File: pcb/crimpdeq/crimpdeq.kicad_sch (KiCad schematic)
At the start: 55 parts, among them J10 A-_Cable_Pad, J11 E+_Cable_Pad, J12 E-_Cable_Pad, J2 USB4105-GF-A, J5 B-_Cable_Pad, J6 SW+_Cable_Pad, J7 B+_Cable_Pad, J8 SW-_Cable_Pad, J9 A+_Cable_Pad, Q2 DMG3415U, U1 ESP32-C3-MINI-1, U2 MCP73831T-2ACI/OT, U3 ADS1220, U5 MAX17048G+T10, U6 SY8088

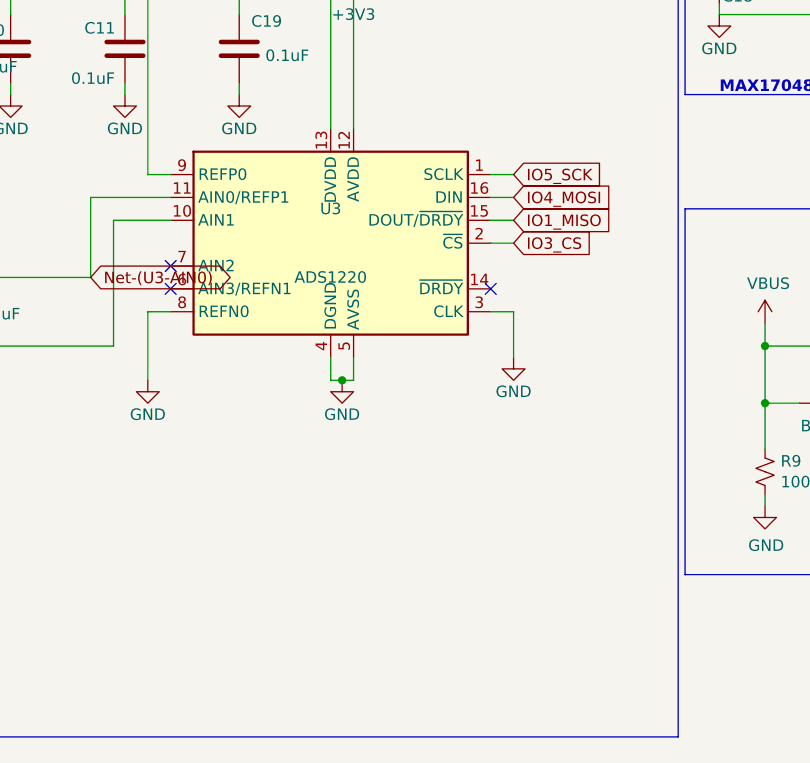
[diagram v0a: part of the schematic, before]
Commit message: fix: add ADC SPI damping and C0G filter
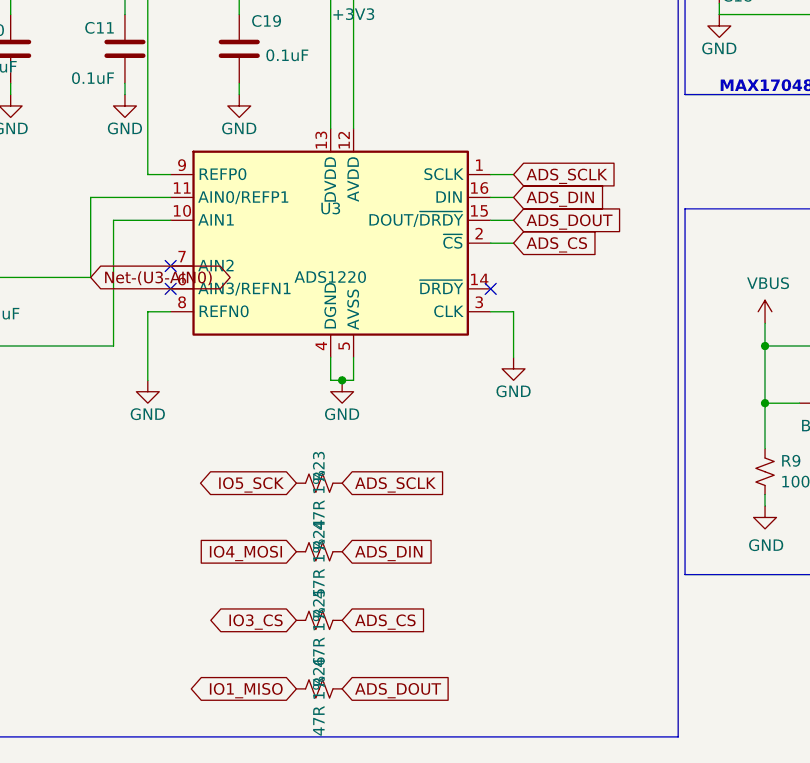
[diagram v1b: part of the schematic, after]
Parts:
- added R23, R24, R25, R26: 47R 1%, Resistor_SMD:R_0402_1005Metric, symbol Device:R_Small_US
- C12: footprint Capacitor_SMD:C_0603_1608Metric -> Capacitor_SMD:C_1206_3216Metric; LCSC (none) -> C405303; MPN (none) -> GRM31C5C2A104JA01L; Manufacturer (none) -> Murata
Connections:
- net IO1_MISO: now also R26.2; no longer U3.15 (DOUT/~{DRDY})
- net IO3_CS: now also R25.1; no longer U3.2 (~{CS})
- net IO4_MOSI: now also R24.1; no longer U3.16 (DIN)
- net IO5_SCK: now also R23.1; no longer U3.1 (SCLK)
- new net ADS_CS: R25.2, U3.2 (~{CS})
- new net ADS_DIN: R24.2, U3.16 (DIN)
- new net ADS_DOUT: R26.1, U3.15 (DOUT/~{DRDY})
- new net ADS_SCLK: R23.2, U3.1 (SCLK)

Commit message: fix: reconcile PCB and schematic libraries
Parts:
- C11, C19: footprint C_0603_1608Metric -> Capacitor_SMD:C_0603_1608Metric
- D4: LCSC (none) -> C52917433; MANUFACTURER (none) -> Worldsemi; MPN (none) -> WS2812B-V6
- J2: footprint Rust_Board:GCT_USB4105-GF-A -> Crimpdeq:GCT_USB4105-GF-A; symbol Rust_Board:USB4105-GF-A -> Crimpdeq:USB4105-GF-A; MPN (none) -> USB4105-GF-A
- Q2: footprint Package_TO_SOT_SMD:SOT-23 -> Crimpdeq:SOT-23; MANUFACTURER (none) -> Diodes Incorporated; MPN (none) -> DMG3415U-7
- U1: footprint PCM_Espressif:ESP32-C3-MINI-1 -> Crimpdeq:ESP32-C3-MINI-1; symbol Espressif:ESP32-C3-MINI-1 -> Crimpdeq:ESP32-C3-MINI-1; MANUFACTURER (none) -> Espressif Systems; MPN (none) -> ESP32-C3-MINI-1
- U2: footprint Package_TO_SOT_SMD:SOT-23-5 -> Crimpdeq:MCP73831_SOT-23-5
- U3: footprint TSSOP-16_4.4x5mm_P0.65mm -> Package_SO:TSSOP-16_4.4x5mm_P0.65mm; LCSC (none) -> C48263; MANUFACTURER (none) -> Texas Instruments; MPN (none) -> ADS1220IPWR
- U5: symbol Battery_Management:MAX17048 -> Crimpdeq:MAX17048; LCSC (none) -> C2682616; MANUFACTURER (none) -> Analog Devices / Maxim Integrated; MPN (none) -> MAX17048G+T10
- U6: footprint Package_TO_SOT_SMD:SOT-23-5 -> Crimpdeq:SY8088_SOT-23-5; symbol Rust_Board:SY8088 -> Crimpdeq:SY8088
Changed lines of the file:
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@@
 			)
 		)
-		(property "Footprint" "Package_TO_SOT_SMD:SOT-23-5"
+		(property "Footprint" "Crimpdeq:MCP73831_SOT-23-5"
 			(at 152.4 43.18 0)
 			(hide yes)
@@
 			)
 		)
-		(property "Footprint" "Package_TO_SOT_SMD:SOT-23"
+		(property "Footprint" "Crimpdeq:SOT-23"
 			(at 151.13 155.575 0)
 			(hide yes)
@@
 			)
 		)
-		(property "Datasheet" "https://www.diodes.com/assets/Datasheets/DMG2301L.pdf"
+		(property "Datasheet" "https://www.diodes.com/assets/Datasheets/DMG3415U.pdf"
 			(at 146.05 153.67 0)
 			(hide yes)
@@
 			)
 		)
-	)
+		(property "MANUFACTURER" "Diodes Incorporated"
+			(at 146.05 153.67 0)
+			(hide yes)
+			(effects
+				(font
+					(size 1.27 1.27)
+				)
+			)
+		)
+		(property "MPN" "DMG3415U-7"
+			(at 146.05 153.67 0)
+			(hide yes)
+			(effects
+				(font
+					(size 1.27 1.27)
+				)
+			)
+		))
 	(symbol
 		(lib_id "Connector_Generic:Conn_01x01")
@@
 			)
 		)
-		(property "Footprint" "TSSOP-16_4.4x5mm_P0.65mm"
+		(property "Footprint" "Package_SO:TSSOP-16_4.4x5mm_P0.65mm"
 			(at 82.55 142.24 0)
 			(hide yes)
@@
 			)
 		)
-		(property "Datasheet" ""
+		(property "Datasheet" "https://www.ti.com/lit/ds/symlink/ads1220.pdf"
 			(at 82.55 142.24 0)
 			(hide yes)
@@
 			)
 		)
-	)
+		(property "LCSC" "C48263"
+			(at 82.55 142.24 0)
+			(hide yes)
+			(effects
+				(font
+					(size 1.27 1.27)
+				)
+			)
+		)
+		(property "MANUFACTURER" "Texas Instruments"
+			(at 82.55 142.24 0)
+			(hide yes)
+			(effects
+				(font
+					(size 1.27 1.27)
+				)
+			)
+		)
+		(property "MPN" "ADS1220IPWR"
+			(at 82.55 142.24 0)
+			(hide yes)
+			(effects
+				(font
+					(size 1.27 1.27)
+				)
+			)
+		))
 	(symbol
 		(lib_id "Device:R_Small_US")
@@
 	)
 	(symbol
-		(lib_id "Espressif:ESP32-C3-MINI-1")
+		(lib_id "Crimpdeq:ESP32-C3-MINI-1")
 		(at 85.09 53.34 0)
 		(unit 1)
@@
 			)
 		)
-		(property "Footprint" "PCM_Espressif:ESP32-C3-MINI-1"
+		(property "Footprint" "Crimpdeq:ESP32-C3-MINI-1"
 			(at 85.09 86.36 0)
 			(hide yes)
@@
 			)
 		)
-	)
+		(property "MANUFACTURER" "Espressif Systems"
+			(at 85.09 53.34 0)
+			(hide yes)
+			(effects
+				(font
+					(size 1.27 1.27)
+				)
+			)
+		)
+		(property "MPN" "ESP32-C3-MINI-1"
+			(at 85.09 53.34 0)
+			(hide yes)
+			(effects
+				(font
+					(size 1.27 1.27)
+				)
+			)
+		))
 	(symbol
 		(lib_id "power:+3V3")
@@
 	)
 	(symbol
-		(lib_id "Rust_Board:SY8088")
+		(lib_id "Crimpdeq:SY8088")
 		(at 226.06 83.82 0)
 		(unit 1)
@@
 			)
 		)
-		(property "Footprint" "Package_TO_SOT_SMD:SOT-23-5"
+		(property "Footprint" "Crimpdeq:SY8088_SOT-23-5"
 			(at 226.06 106.68 0)
 			(hide yes)
@@
 	)
 	(symbol
-		(lib_id "Rust_Board:USB4105-GF-A")
+		(lib_id "Crimpdeq:USB4105-GF-A")
 		(at 213.36 39.37 0)
 		(unit 1)
@@
 			)
 		)
-		(property "Footprint" "Rust_Board:GCT_USB4105-GF-A"
+		(property "Footprint" "Crimpdeq:GCT_USB4105-GF-A"
 			(at 220.98 64.77 0)
 			(hide yes)
@@
 			)
 		)
-		(property "Datasheet" ""
+		(property "Datasheet" "https://gct.co/files/drawings/usb4105.pdf"
 			(at 212.09 34.29 0)
 			(hide yes)
@@
 			)
 		)
-	)
+		(property "MPN" "USB4105-GF-A"
+			(at 213.36 39.37 0)
+			(hide yes)
+			(effects
+				(font
+					(size 1.27 1.27)
+				)
+			)
+		))
 	(symbol
 		(lib_id "power:GND")
@@
 			)
 		)
-		(property "Footprint" "C_0603_1608Metric"
+		(property "Footprint" "Capacitor_SMD:C_0603_1608Metric"
 			(at 59.69 120.65 0)
 			(hide yes)
@@
 			)
 		)
-		(property "Footprint" "C_0603_1608Metric"
+		(property "Footprint" "Capacitor_SMD:C_0603_1608Metric"
 			(at 72.39 120.65 0)
 			(hide yes)
@@
 			)
 		)
-		(property "Datasheet" "https://cdn-shop.adafruit.com/datasheets/WS2812B.pdf"
+		(property "Datasheet" "https://www.lcsc.com/datasheet/C52917433.pdf"
 			(at 149.86 85.725 0)
 			(hide yes)
@@
 			)
 		)
-	)
+		(property "LCSC" "C52917433"
+			(at 147.32 76.2 0)
+			(hide yes)
+			(effects
+				(font
+					(size 1.27 1.27)
+				)
+			)
+		)
+		(property "MANUFACTURER" "Worldsemi"
+			(at 147.32 76.2 0)
+			(hide yes)
+			(effects
+				(font
+					(size 1.27 1.27)
+				)
+			)
+		)
+		(property "MPN" "WS2812B-V6"
+			(at 147.32 76.2 0)
+			(hide yes)
+			(effects
+				(font
+					(size 1.27 1.27)
+				)
+			)
+		))
 	(symbol
 		(lib_id "Device:R_Small_US")
@@
 	)
 	(symbol
-		(lib_id "Battery_Management:MAX17048")
+		(lib_id "Crimpdeq:MAX17048")
 		(at 149.86 111.76 0)
 		(unit 1)
@@
 			)
 		)
-		(property "Datasheet" ""
+		(property "Datasheet" "https://www.analog.com/media/en/technical-documentation/data-sheets/MAX17048-MAX17049.pdf"
 			(at 149.86 111.76 0)
 			(hide yes)
@@
 			)
 		)
-	)
+		(property "LCSC" "C2682616"
+			(at 149.86 111.76 0)
+			(hide yes)
+			(effects
+				(font
+					(size 1.27 1.27)
+				)
+			)
+		)
+		(property "MANUFACTURER" "Analog Devices / Maxim Integrated"
+			(at 149.86 111.76 0)
+			(hide yes)
+			(effects
+				(font
+					(size 1.27 1.27)
+				)
+			)
+		)
+		(property "MPN" "MAX17048G+T10"
+			(at 149.86 111.76 0)
+			(hide yes)
+			(effects
+				(font
+					(size 1.27 1.27)
+				)
+			)
+		))
 	(symbol
 		(lib_id "Device:R_Small_US")

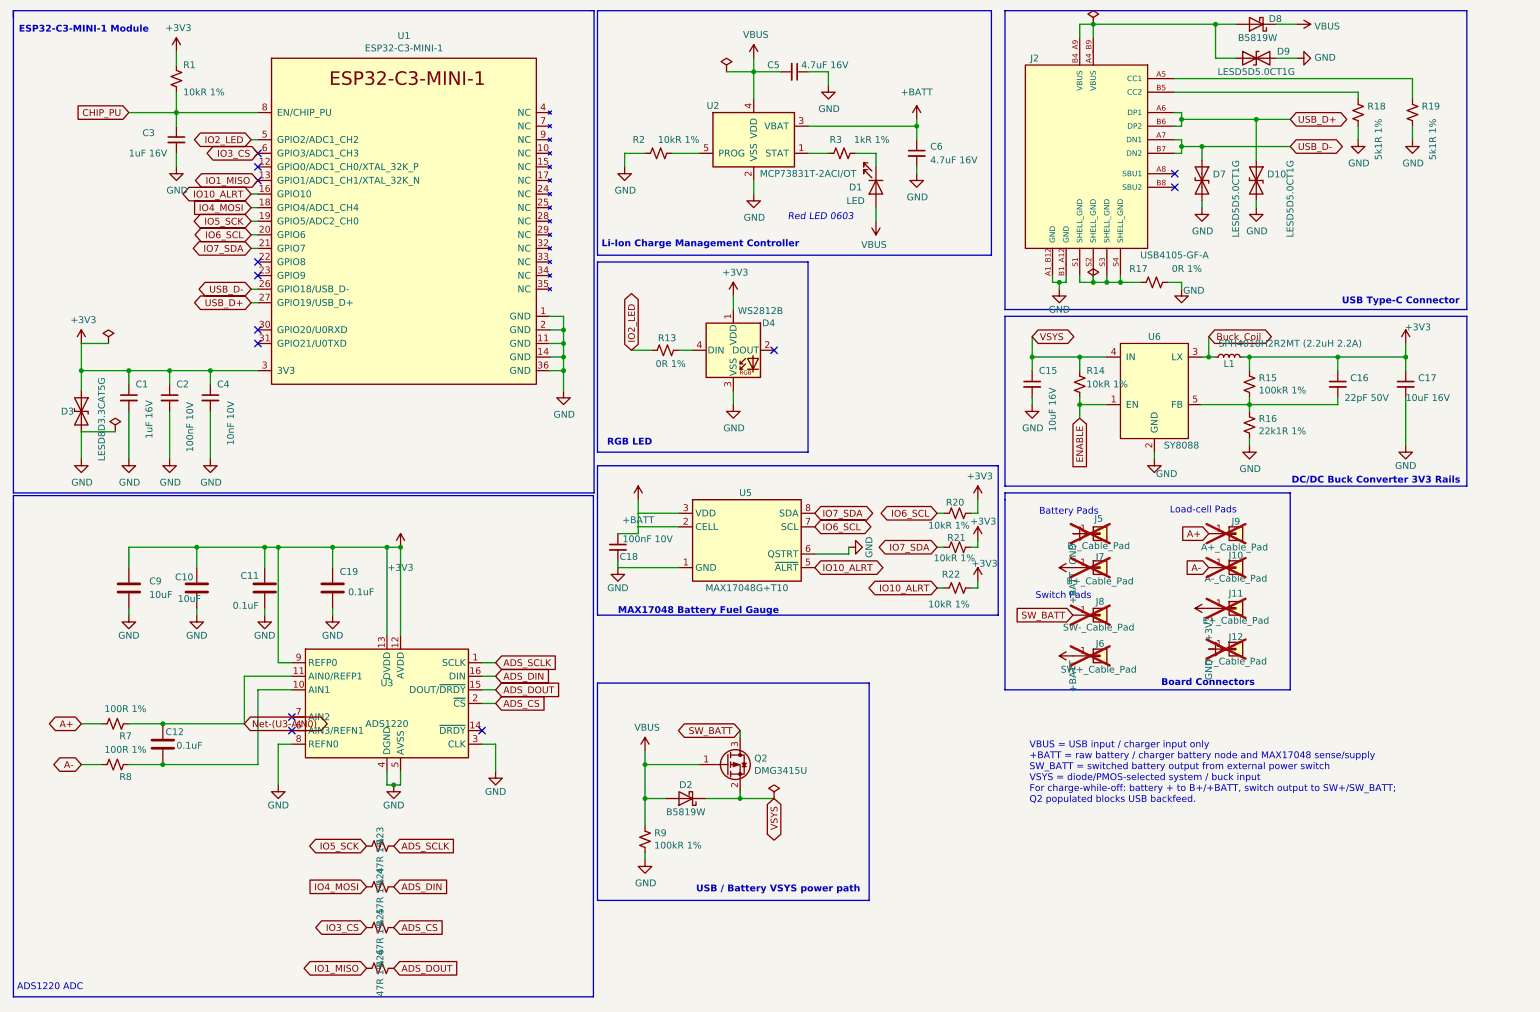
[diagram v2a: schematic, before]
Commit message: Revert "Revision 3 (#26)"
This reverts commit 90a500b67033c502f14e333f57f99a449d93ac6c.
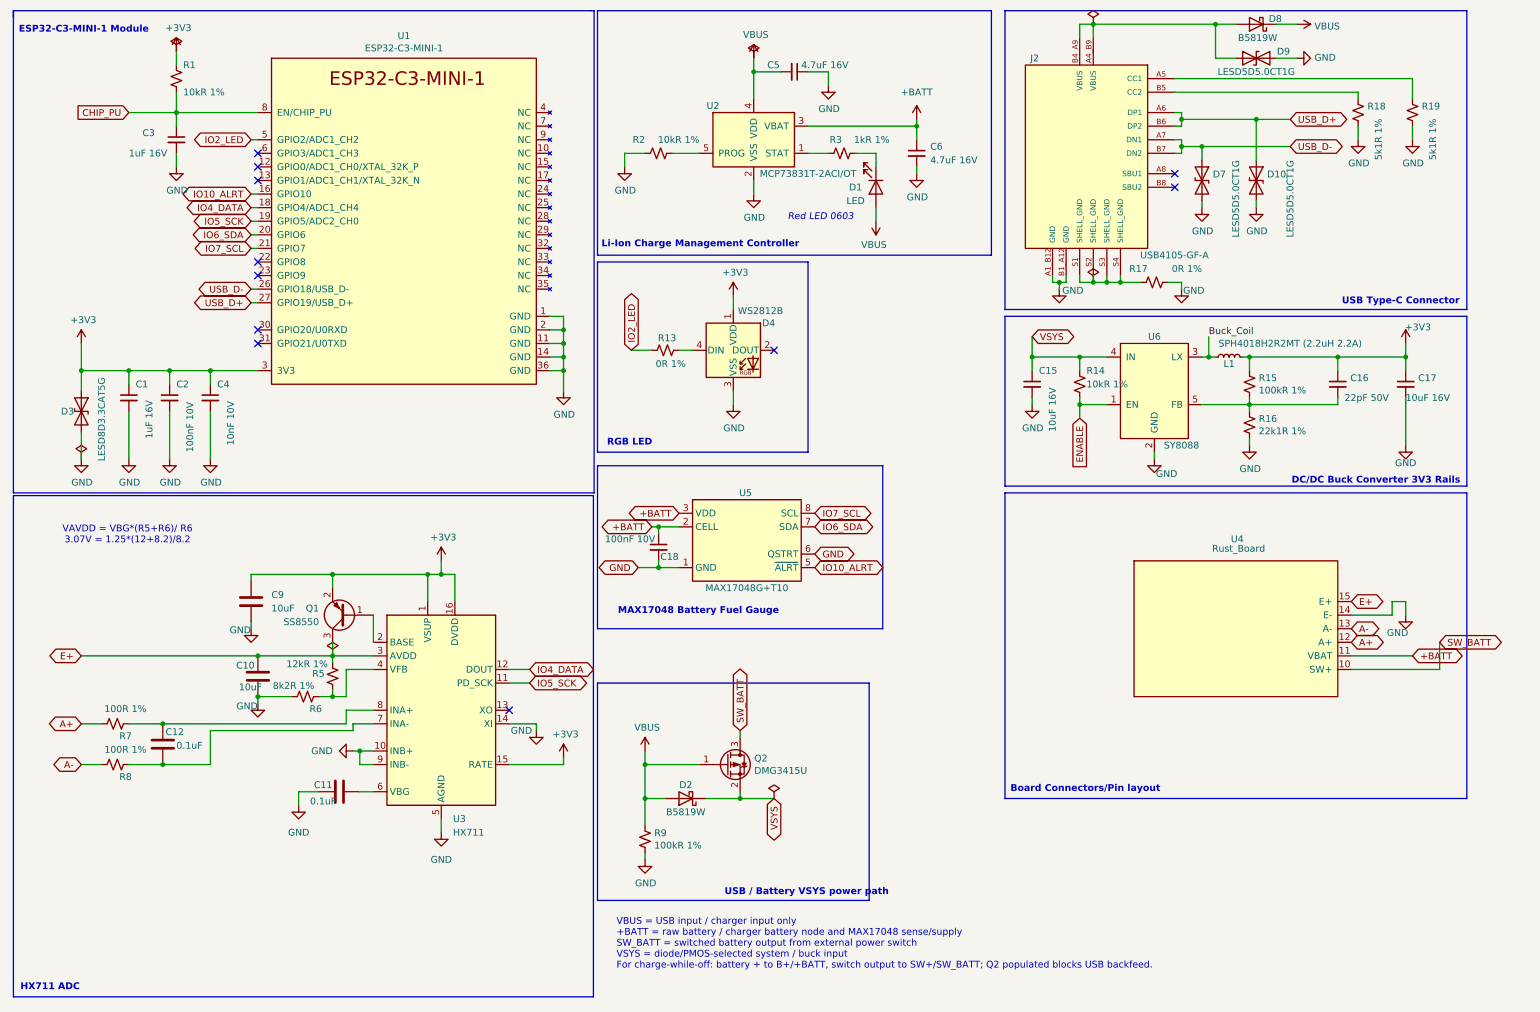
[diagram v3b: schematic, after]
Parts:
- removed C19: 0.1uF, Capacitor_SMD:C_0603_1608Metric, symbol Device:C
- removed J10: A-_Cable_Pad, TestPoint:TestPoint_THTPad_D1.5mm_Drill0.7mm, symbol Connector_Generic:Conn_01x01
- removed J11: E+_Cable_Pad, TestPoint:TestPoint_THTPad_D1.5mm_Drill0.7mm, symbol Connector_Generic:Conn_01x01
- removed J12: E-_Cable_Pad, TestPoint:TestPoint_THTPad_D1.5mm_Drill0.7mm, symbol Connector_Generic:Conn_01x01
- removed J5: B-_Cable_Pad, TestPoint:TestPoint_THTPad_D1.5mm_Drill0.7mm, symbol Connector_Generic:Conn_01x01
- removed J6: SW+_Cable_Pad, TestPoint:TestPoint_THTPad_D1.5mm_Drill0.7mm, symbol Connector_Generic:Conn_01x01
- removed J7: B+_Cable_Pad, TestPoint:TestPoint_THTPad_D1.5mm_Drill0.7mm, symbol Connector_Generic:Conn_01x01
- removed J8: SW-_Cable_Pad, TestPoint:TestPoint_THTPad_D1.5mm_Drill0.7mm, symbol Connector_Generic:Conn_01x01
- removed J9: A+_Cable_Pad, TestPoint:TestPoint_THTPad_D1.5mm_Drill0.7mm, symbol Connector_Generic:Conn_01x01
- removed R20, R21, R22: 10kR 1%, Resistor_SMD:R_0402_1005Metric, symbol Device:R_Small_US
- removed R23, R24, R25, R26: 47R 1%, Resistor_SMD:R_0402_1005Metric, symbol Device:R_Small_US
- removed U3: ADS1220, Package_SO:TSSOP-16_4.4x5mm_P0.65mm, symbol Analog_ADC:ADS1220xPW
- added Q1: SS8550, Package_TO_SOT_SMD:SOT-23, symbol Transistor_BJT:SS8550
- added R5: 12kR 1%, Resistor_SMD:R_0402_1005Metric, symbol Device:R_Small_US
- added R6: 8k2R 1%, Resistor_SMD:R_0402_1005Metric, symbol Device:R_Small_US
- added U3: HX711, Package_SO:SOP-16_3.9x9.9mm_P1.27mm, symbol Analog_ADC:HX711
- added U4: Rust_Board, symbol Rust_Board:Rust_Board
- C12: footprint Capacitor_SMD:C_1206_3216Metric -> Capacitor_SMD:C_0603_1608Metric; LCSC C405303 -> (none); MPN GRM31C5C2A104JA01L -> (none); Manufacturer Murata -> (none)
- D4: LCSC C52917433 -> (none); MANUFACTURER Worldsemi -> (none); MPN WS2812B-V6 -> (none)
- J2: footprint Crimpdeq:GCT_USB4105-GF-A -> Rust_Board:GCT_USB4105-GF-A; symbol Crimpdeq:USB4105-GF-A -> Rust_Board:USB4105-GF-A; MPN USB4105-GF-A -> (none)
- Q2: footprint Crimpdeq:SOT-23 -> Package_TO_SOT_SMD:SOT-23; symbol Transistor_FET:Q_PMOS_GSD -> Transistor_FET:DMG2301L; MANUFACTURER Diodes Incorporated -> (none); MPN DMG3415U-7 -> (none)
- R7, R8: LCSC C25076 -> C25741
- U1: footprint Crimpdeq:ESP32-C3-MINI-1 -> PCM_Espressif:ESP32-C3-MINI-1; symbol Crimpdeq:ESP32-C3-MINI-1 -> Espressif:ESP32-C3-MINI-1; MANUFACTURER Espressif Systems -> (none); MPN ESP32-C3-MINI-1 -> (none)
- U2: footprint Crimpdeq:MCP73831_SOT-23-5 -> Package_TO_SOT_SMD:SOT-23-5
- U5: symbol Crimpdeq:MAX17048 -> Battery_Management:MAX17048; LCSC C2682616 -> (none); MANUFACTURER Analog Devices / Maxim Integrated -> (none); MPN MAX17048G+T10 -> (none)
- U6: footprint Crimpdeq:SY8088_SOT-23-5 -> Package_TO_SOT_SMD:SOT-23-5; symbol Crimpdeq:SY8088 -> Rust_Board:SY8088
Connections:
- net +3V3: now also Q1.2 (E), U3.1 (VSUP), U3.15 (RATE), U3.16 (DVDD); no longer C10.1, C11.1
- net +BATT: now also U4.11 (VBAT)
- net A+: now also U4.12 (A+)
- net A-: now also U4.13 (A-)
- net GND: now also C11.1, R6.2, U3.10 (INB+), U3.14 (XI), U3.5 (AGND), U3.9 (INB-), U4.14 (E-); no longer C11.2, U1.37 (GND), U1.38 (GND), U1.39 (GND), U1.40 (GND), U1.41 (GND), U1.42 (GND), U1.43 (GND), U1.44 (GND), U1.45 (GND), U1.46 (GND), U1.47 (GND), U1.48 (GND), U1.49 (GND), U1.50 (GND), U1.51 (GND), U1.52 (GND), U1.53 (GND)
- net IO5_SCK: now also U3.11 (PD_SCK)
- net SW_BATT: now also U4.10 (SW+)
- net at C12.2, R8.1: now also U3.7 (INA-)
- net IO1_MISO: no longer names the net of U1.13 (GPIO1/ADC1_CH1/XTAL_32K_N)
- net IO3_CS: no longer names the net of U1.6 (GPIO3/ADC1_CH3)
- net IO4_MOSI renamed IO4_DATA
- net IO4_DATA: now also U3.12 (DOUT)
- net IO6_SCL renamed IO6_SDA
- net IO7_SDA renamed IO7_SCL
- net Net-(U3-AIN0): no longer names the net of C12.1, R7.1
- net Net-(U3-AIN0): now also U3.8 (INA+)
- new net: R5.2, R6.1, U3.4 (VFB)
- new net: C11.2, U3.6 (VBG)
- new net: Q1.1 (B), U3.2 (BASE)
- new net E+: C10.1, Q1.3 (C), R5.1, U3.3 (AVDD), U4.15 (E+)
- no-connect marks 13 -> 11
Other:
- note added: "Board Connectors/Pin layout"
- note added: "HX711 ADC"
- note added: "VAVDD = VBG*(R5+R6)/ R6 3.07V = 1.25*(12+8.2)/8.2"
- note removed: "ADS1220 ADC"
- note removed: "Battery Pads"
- note removed: "Board Connectors"
- note removed: "Load-cell Pads"
- note removed: "Switch Pads"
- moved on the sheet: C10, C18, C9
